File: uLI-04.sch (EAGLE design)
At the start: 40 parts, among them IC1 PIC18F14K50-I/SS, IC2 ADM2483, IC3 MCP130T, IC4 78L05F, J1 PICPROG2-V, J5 WEBP6, J6 WEBP6, J7 WEBP6, Q1 12.00 MHz, T1 IRF7306, X1 MINI-USB_SHIELD4P-USB-SPEC, X2 ARK1550/2_S

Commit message: Change value of LED resistors based on reality.
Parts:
- R11: value 10k -> 2k2
- R8: value 10k -> 100k

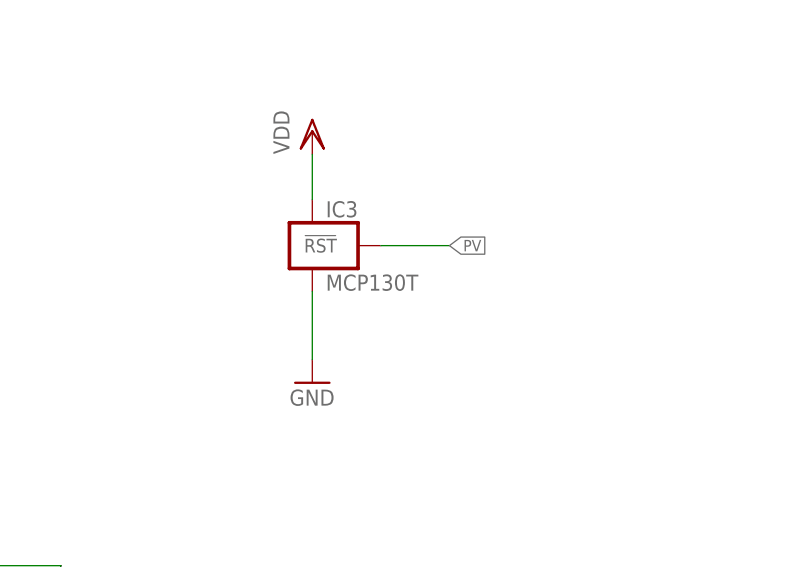
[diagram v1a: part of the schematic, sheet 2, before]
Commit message: Set precise MCP's voltage.
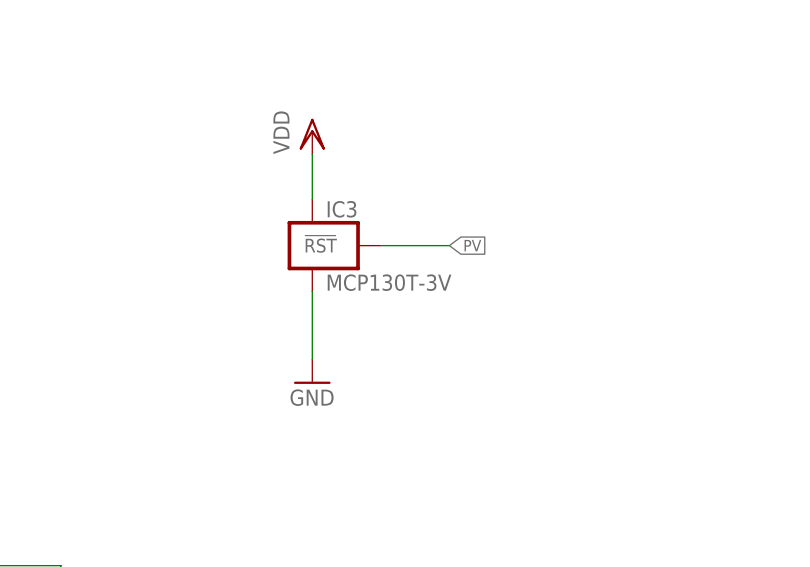
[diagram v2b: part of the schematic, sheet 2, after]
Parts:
- IC3: value MCP130T -> MCP130T-3V
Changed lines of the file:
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@@
 <part name="VDD4" library="supply1" deviceset="VDD" device=""/>
 <part name="GND14" library="supply1" deviceset="GND" device=""/>
-<part name="IC3" library="my" deviceset="MCP130T" device=""/>
+<part name="IC3" library="my" deviceset="MCP130T" device="" value="MCP130T-3V"/>
 <part name="R12" library="rcl" deviceset="R-EU_" device="R1206" value="2k2"/>
 <part name="GND15" library="supply1" deviceset="GND" device=""/>
